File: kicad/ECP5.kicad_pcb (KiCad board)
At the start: 4 copper layers, 64.4 x 54.6 mm, 143 parts, among them J1 USB Type C, J2 USB Type C, J3 FTS-126-02-L-DV, Q1 MMST2222A, SW1 User, U1 LFE5U-25F-6BG381C, U2 IS25LP128F, U3 FT231XQ, U4 LP5907MFX-3.3, U5 FT2232HQ, U6 93LCxxBxxOT, U7 TLV62569DBVT, U8 TLV62569DBVT, U9 TLV62569DBVT, Y1 50MHz, Y2 12.000 MHz

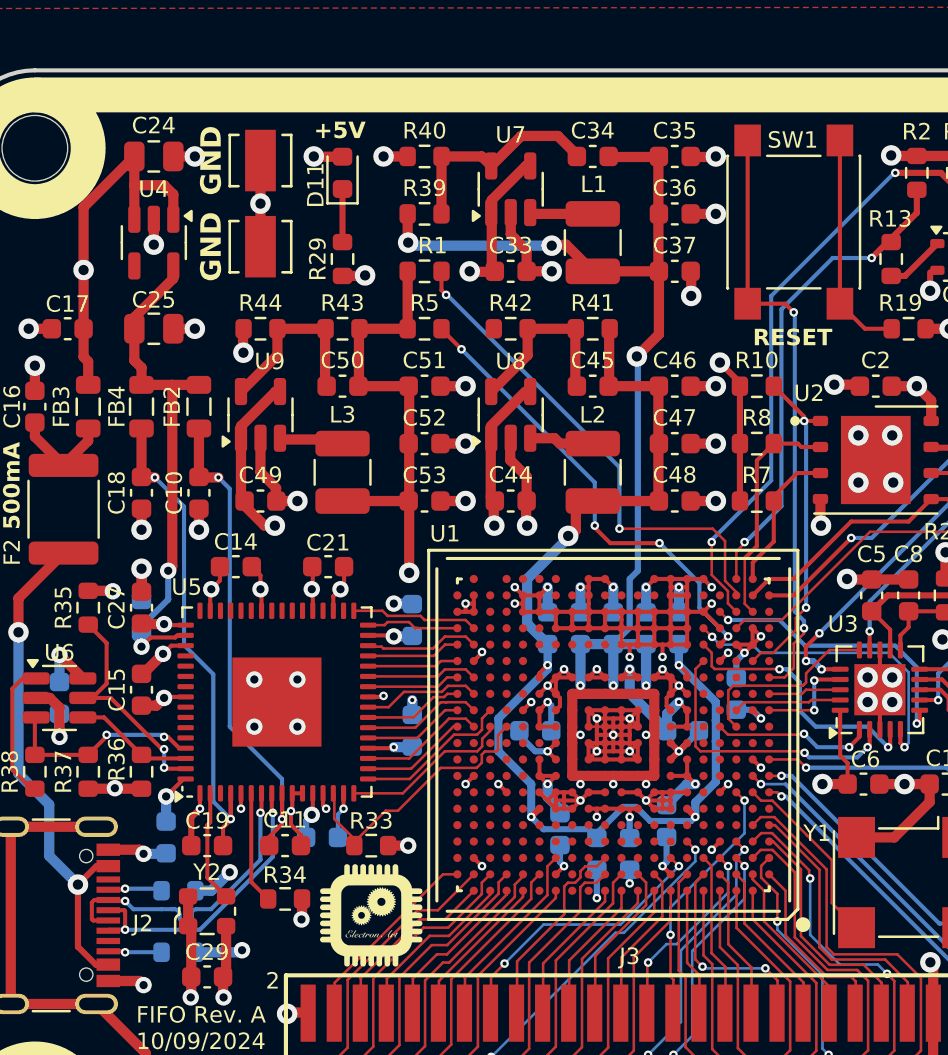
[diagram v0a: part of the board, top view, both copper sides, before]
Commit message: Updated USB D+/- routing
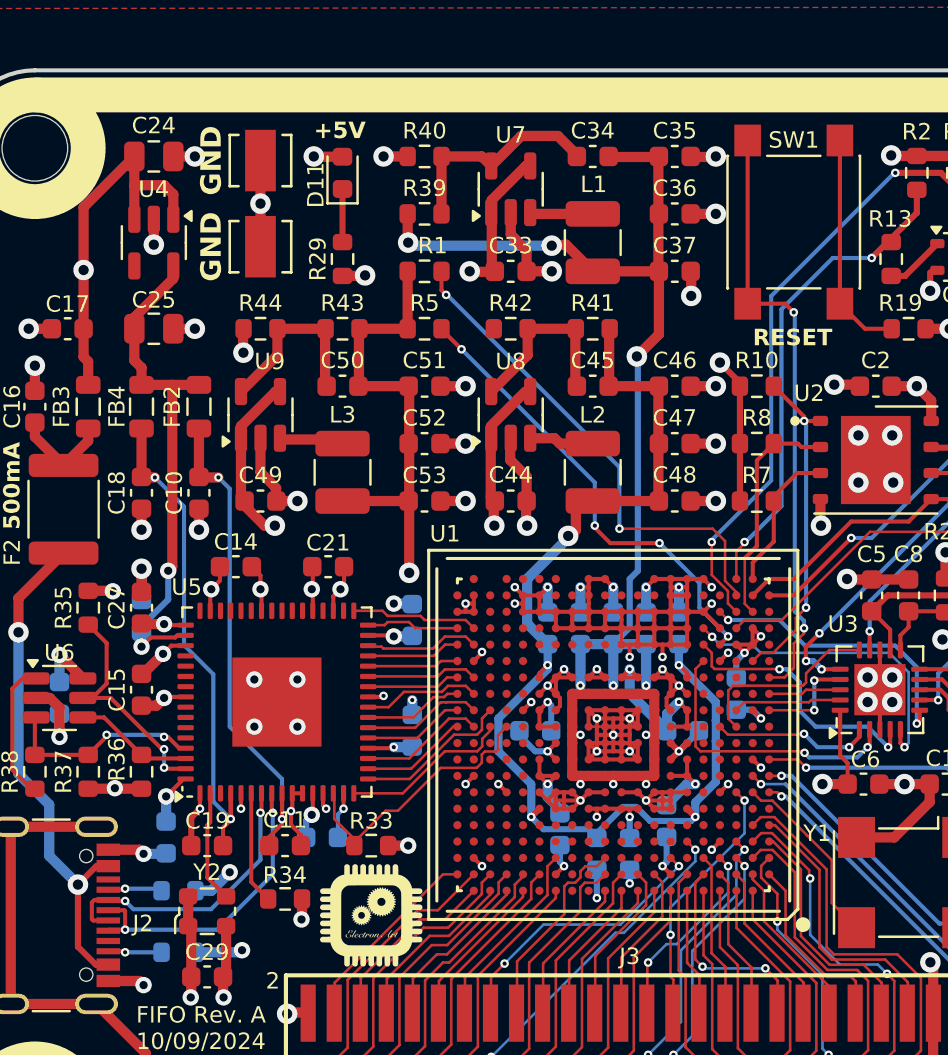
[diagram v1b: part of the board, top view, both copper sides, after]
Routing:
- net FTDI_D-: track 15.1 -> 14.4 mm
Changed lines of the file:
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@@
 		(tags "SPST Button Switch")
 		(property "Reference" "SW1"
-			(at -4 0.05 0)
+			(at -4 0 0)
 			(unlocked yes)
 			(layer "F.SilkS")
@@
 		)
 		(property "Value" "0.1µF"
-			(at 0 1.43 360)
+			(at 0 1.43 0)
 			(layer "F.Fab")
 			(effects
@@
 		)
 		(fp_text user "${REFERENCE}"
-			(at 0 0 360)
+			(at 0 0 0)
 			(layer "F.Fab")
 			(effects
@@
 		)
 		(property "Value" "2.2K"
-			(at 0 1.43 360)
+			(at 0 1.43 0)
 			(layer "F.Fab")
 			(effects
@@
 		)
 		(fp_text user "${REFERENCE}"
-			(at 0 0 360)
+			(at 0 0 0)
 			(layer "F.Fab")
 			(effects
@@
 		)
 		(fp_text user "${REFERENCE}"
-			(at 0 0 360)
+			(at 0 0 0)
 			(layer "F.Fab")
 			(effects
@@
 		)
 		(property "Value" "0.1µF"
-			(at 0 1.43 360)
+			(at 0 1.43 0)
 			(layer "F.Fab")
 			(effects
@@
 		)
 		(property "Value" "0.1µF"
-			(at 0 1.43 360)
+			(at 0 1.43 0)
 			(layer "F.Fab")
 			(effects
@@
 		)
 		(fp_text user "${REFERENCE}"
-			(at 0 0 360)
+			(at 0 0 0)
 			(layer "F.Fab")
 			(effects
@@
 		)
 		(property "Value" "0.1µF"
-			(at 0 1.43 360)
+			(at 0 1.43 0)
 			(layer "F.Fab")
 			(effects
@@
 		)
 		(fp_text user "${REFERENCE}"
-			(at 0 0 360)
+			(at 0 0 0)
 			(layer "F.Fab")
 			(effects
@@
 		)
 		(property "Value" "93LCxxBxxOT"
-			(at 0 2.4 360)
+			(at 0 2.4 0)
 			(layer "F.Fab")
 			(effects
@@
 		)
 		(fp_text user "${REFERENCE}"
-			(at 0 0 360)
+			(at 0 0 0)
 			(layer "F.Fab")
 			(effects
@@
 		)
 		(property "Value" "5.1K"
-			(at 0 -1.43 360)
+			(at 0 -1.43 0)
 			(layer "B.Fab")
 			(effects
@@
 		)
 		(property "Value" "0.1µF"
-			(at 0 -1.43 360)
+			(at 0 -1.43 0)
 			(layer "B.Fab")
 			(effects
@@
 		)
 		(fp_text user "${REFERENCE}"
-			(at 0 0 360)
+			(at 0 0 0)
 			(layer "B.Fab")
 			(effects
@@
 		)
 		(property "Value" "5.1K"
-			(at 0 -1.43 360)
+			(at 0 -1.43 0)
 			(layer "B.Fab")
 			(effects
@@
 	)
 	(segment
-		(start 122.606552 110.3)
-		(end 122.486552 110.3)
-		(width 0.2)
-		(layer "B.Cu")
-		(net 232)
-	)
-	(segment
-		(start 122.846552 110.66)
-		(end 122.846552 110.54)
-		(width 0.2)
-		(layer "B.Cu")
-		(net 232)
-	)
-	(segment
-		(start 122.486552 110.3)
-		(end 121.992515 110.3)
-		(width 0.2)
-		(layer "B.Cu")
-		(net 232)
-	)
-	(segment
-		(start 126.8 107.886712)
-		(end 124.386712 110.3)
-		(width 0.2)
-		(layer "B.Cu")
-		(net 232)
-	)
-	(segment
 		(start 120.6 110.3)
 		(end 120.2 109.9)
@@
 	)
 	(segment
-		(start 121.992515 110.3)
-		(end 120.6 110.3)
-		(width 0.2)
-		(layer "B.Cu")
-		(net 232)
-	)
-	(segment
-		(start 123.446552 110.54)
-		(end 123.446552 110.66)
-		(width 0.2)
-		(layer "B.Cu")
-		(net 232)
-	)
-	(segment
-		(start 123.206552 110.9)
-		(end 123.086552 110.9)
-		(width 0.2)
-		(layer "B.Cu")
-		(net 232)
-	)
-	(segment
-		(start 124.386712 110.3)
-		(end 123.686552 110.3)
+		(start 126.8 107.886712)
+		(end 124.386712 110.3)
 		(width 0.2)
 		(layer "B.Cu")
@@
 		(net 232)
 	)
-	(arc
-		(start 122.846552 110.54)
-		(mid 122.776258 110.370294)
-		(end 122.606552 110.3)
-		(width 0.2)
-		(layer "B.Cu")
-		(net 232)
-	)
-	(arc
-		(start 123.446552 110.66)
-		(mid 123.376258 110.829706)
-		(end 123.206552 110.9)
-		(width 0.2)
-		(layer "B.Cu")
-		(net 232)
-	)
-	(arc
-		(start 123.686552 110.3)
-		(mid 123.516846 110.370294)
-		(end 123.446552 110.54)
-		(width 0.2)
-		(layer "B.Cu")
-		(net 232)
-	)
-	(arc
-		(start 123.086552 110.9)
-		(mid 122.916846 110.829706)
-		(end 122.846552 110.66)
+	(segment
+		(start 124.386712 110.3)
+		(end 120.6 110.3)
 		(width 0.2)
 		(layer "B.Cu")
@@
 	)
 	(segment
-		(start 127.4 107.74916)
-		(end 123.84916 111.3)
-		(width 0.2)
-		(layer "B.Cu")
-		(net 233)
-	)
-	(segment
-		(start 123.84916 111.3)
+		(start 124.7 111.3)
 		(end 120.2 111.3)
 		(width 0.2)
@@
 	)
 	(segment
-		(start 127.4 105.582695)
-		(end 127.4 107.74916)
+		(start 127.4 108.6)
+		(end 124.7 111.3)
 		(width 0.2)
 		(layer "B.Cu")
@@
 	(segment
 		(start 127.4 105.6)
-		(end 127.4 105.582695)
+		(end 127.4 108.6)
 		(width 0.2)
 		(layer "B.Cu")
@@
 		)
 	)
-	(generated
-		(type tuning_pattern)
-		(name "Tuning Pattern")
-		(layer "B.Cu")
-		(base_line
-			(pts
-				(xy 123.686552 110.3) (xy 121.992515 110.3)
-			)
-		)
-		(corner_radius_percent 80)
-		(end
-			(xy 121.992515 110.3)
-		)
-		(initial_side "left")
-		(last_diff_pair_gap 0.18)
-		(last_netname "FTDI_D-")
-		(last_status "too_short")
-		(last_track_width 0.2)
-		(last_tuning "15.6827 mm (too short)")
-		(max_amplitude 0.6)
-		(min_amplitude 0)
-		(min_spacing 0.6)
-		(origin
-			(xy 123.686552 110.3)
-		)
-		(override_custom_rules no)
-		(rounded yes)
-		(single_sided no)
-		(target_length 1000000)
-		(target_length_max 1000000.1)
-		(target_length_min 999999.9)
-		(target_skew 0)
-		(target_skew_max 0.1)
-		(target_skew_min -0.1)
-		(tuning_mode "single")
-		(members 2487f087-3aac-4a66-bda5-6327e1fa3f22 2b26a126-b3eb-435b-8f4a-f1089f99072d
-			36cd9a7a-7935-4e43-ac3e-73e7b1a5498a 40a33053-0dbd-45e0-8974-fa353c070704
-			84474866-c306-4e32-822d-058b60b3c7e6 8e153df2-7bb3-4bf4-a8ca-de7ae37abfcd
-			aaa3d956-0208-4fe1-a436-eeab9a2938b5 cbec4b23-d0f2-4299-8d58-a59de2e950d6
-			ec4c1b6e-fc9b-46a4-91a6-a9cc44f7a438
-		)
-	)

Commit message: Routing complete
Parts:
- added C2: 0.1µF, Capacitor_SMD:C_0603_1608Metric, F.Cu at (166.8, 107.2)
- added Y2: 22.5792 MHz, Oscillator:Oscillator_SMD_Abracon_ASE-4Pin_3.2x2.5mm, F.Cu at (163.2, 107.2)
- F1: value Hold 750mA -> Hold 140mA
- Y1: value 50MHz -> 24.576 MHz; footprint ECP5_TX_AUDIO:Oscillator_SMD_Diodes_FN-4Pin_7.0x5.0mm -> Oscillator:Oscillator_SMD_Abracon_ASE-4Pin_3.2x2.5mm
- moved C10 4.62 mm to (164.6, 111.2)
- moved R25 3.25 mm to (167.4, 111.2)
- moved C1 3.06 mm to (159.6, 107.2), turned to 90 degrees
- moved Y1 2.84 mm to (156.2, 107.2), turned to 90 degrees
- renumbered C9 to C10, C10 to C11, C11 to C12, C12 to C13, C13 to C14, C14 to C15, C15 to C16, C16 to C17, C17 to C18, C18 to C19, C19 to C20, C20 to C21, C21 to C22, C22 to C23, C23 to C24, C24 to C25, C25 to C26, C26 to C27, C27 to C28, C28 to C29, C2 to C3, C29 to C30, C30 to C31, C31 to C32, C32 to C33, C33 to C34, C34 to C35, C35 to C36, C36 to C37, C37 to C38, C38 to C39, C3 to C4, C39 to C40, C40 to C41, C41 to C42, C42 to C43, C43 to C44, C44 to C45, C45 to C46, C46 to C47, C47 to C48, C48 to C49, C4 to C5, C49 to C50, C50 to C51, C51 to C52, C52 to C53, C53 to C54, C54 to C55, C55 to C56, C56 to C57, C5 to C6, C6 to C7, C7 to C8, C8 to C9, D7 to D5, D5 to D6, D6 to D7, R20 to R19, R21 to R20, R19 to R21, Y2 to Y3
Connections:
- net CLK_50MHz renamed CLK_24.576MHz
- U1 pad F1: unconnected-(U1F-PL26B-PadF1) -> LED_2
- U1 pad H2: LED_2 -> CLK_22.5792MHz
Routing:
- net CLK_22.5792MHz: track 0.00 -> 12.8 mm
- net CLK_24.576MHz: track 9.02 -> 5.22 mm
- net +3V3: track 116.1 -> 118.9 mm, vias 27 -> 28
- net EXT_1: track 19.8 -> 18.2 mm
- net EXT_0: track 13.6 -> 12.1 mm
- net LED_2: track 18.8 -> 17.6 mm, vias 2 -> 0
- net Net-(J1-SHIELD): track 27.4 -> 26.2 mm
- net EXT_3: track 17.7 -> 16.7 mm, vias 2 -> 0
- net EXT_2: track 11.7 -> 10.7 mm
- net EXT_5: track 16.1 -> 15.3 mm
- net GND: track 267.1 -> 267.9 mm
- net EXT_4: track 9.17 -> 8.48 mm
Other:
- board text added: "USB Audio Rev. A 10/09/2024"
- board text removed: "FIFO Rev. A 10/09/2024"

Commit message: PCB changes
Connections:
- net FT2232_RESET renamed ~{FT2232_RESET}
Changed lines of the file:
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@@
 	(net 306 "unconnected-(U5-~{PWREN}-Pad60)")
 	(net 307 "Net-(U5-OSCI)")
-	(net 308 "FT2232_RESET")
+	(net 308 "~{FT2232_RESET}")
 	(net 309 "Net-(D3-A)")
 	(net 310 "Net-(D4-A)")
@@
 		(tags "SOT TO_SOT_SMD")
 		(property "Reference" "U9"
-			(at 2.6 0.45 0)
+			(at 2.6 0.4 0)
 			(unlocked yes)
 			(layer "F.SilkS")
@@
 			(layers "F.Cu" "F.Paste" "F.Mask")
 			(roundrect_rratio 0.25)
-			(net 308 "FT2232_RESET")
+			(net 308 "~{FT2232_RESET}")
 			(pintype "passive")
 		)
@@
 		(tags "capacitor")
 		(property "Reference" "C10"
-			(at 0.6 1.3 90)
+			(at 0 1.3 90)
 			(unlocked yes)
 			(layer "F.SilkS")
@@
 			(size 0.4 0.4)
 			(layers "F.Cu" "F.Paste" "F.Mask")
-			(net 308 "FT2232_RESET")
+			(net 308 "~{FT2232_RESET}")
 			(pinfunction "PR29B")
 			(pintype "bidirectional")
@@
 			(layers "F.Cu" "F.Paste" "F.Mask")
 			(roundrect_rratio 0.25)
-			(net 308 "FT2232_RESET")
+			(net 308 "~{FT2232_RESET}")
 			(pinfunction "~{RESET}")
 			(pintype "input")
@@
 		(tags "SOT TO_SOT_SMD")
 		(property "Reference" "U6"
-			(at 0 -2.2 0)
+			(at 1.1 -2.2 0)
 			(unlocked yes)
 			(layer "F.SilkS")
@@
 		(tags "resistor")
 		(property "Reference" "R31"
-			(at 0 1.4 180)
+			(at 0 1.3 180)
 			(unlocked yes)
 			(layer "B.SilkS")
@@
 		(tags "resistor")
 		(property "Reference" "R32"
-			(at 0 1.43 180)
+			(at 0 1.3 180)
 			(unlocked yes)
 			(layer "B.SilkS")

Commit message: Changed the name of the project path
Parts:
- F1, F2: footprint ECP5_TX_AUDIO:Fuse_1812_4532Metric -> ECP5_BGA381_FT2232HQ_FIFO:Fuse_1812_4532Metric
- J1, J2: footprint ECP5_TX_AUDIO:USB_C_Receptacle_GCT_USB4105-xx-A_16P_TopMnt_Horizontal -> ECP5_BGA381_FT2232HQ_FIFO:USB_C_Receptacle_GCT_USB4105-xx-A_16P_TopMnt_Horizontal
- J3: footprint ECP5_TX_AUDIO:SAMTEC-FTS-126-02-X-DV -> ECP5_BGA381_FT2232HQ_FIFO:SAMTEC-FTS-126-02-X-DV
- TP1, TP2: footprint ECP5_TX_AUDIO:KEYSTONE_5197TR -> ECP5_BGA381_FT2232HQ_FIFO:KEYSTONE_5197TR
- U1: footprint ECP5_TX_AUDIO:BGA-381_pitch0.8mm_dia0.4mm -> ECP5_BGA381_FT2232HQ_FIFO:BGA-381_pitch0.8mm_dia0.4mm
- U2: footprint ECP5_TX_AUDIO:WSON-8-1EP_6x5mm_P1.27mm_EP3.4x4.3mm -> ECP5_BGA381_FT2232HQ_FIFO:WSON-8-1EP_6x5mm_P1.27mm_EP3.4x4.3mm
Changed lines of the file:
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@@
 		)
 	)
-	(footprint "ECP5_TX_AUDIO:WSON-8-1EP_6x5mm_P1.27mm_EP3.4x4.3mm"
+	(footprint "ECP5_BGA381_FT2232HQ_FIFO:WSON-8-1EP_6x5mm_P1.27mm_EP3.4x4.3mm"
 		(layer "F.Cu")
 		(at 156.8 88.4)
@@
 			)
 		)
-		(property "Footprint" "ECP5_TX_AUDIO:WSON-8-1EP_6x5mm_P1.27mm_EP3.4x4.3mm"
+		(property "Footprint" "ECP5_BGA381_FT2232HQ_FIFO:WSON-8-1EP_6x5mm_P1.27mm_EP3.4x4.3mm"
 			(at 0 0 0)
 			(layer "F.Fab")
@@
 			(pintype "power_in")
 		)
-		(model "${ECP5_TX_AUDIO}/3dmodels/WSON8-6x5.STEP"
+		(model "${ECP5_BGA381_FT2232HQ_FIFO}/3dmodels/WSON8-6x5.STEP"
 			(offset
 				(xyz 0 0 0)
@@
 		)
 	)
-	(footprint "ECP5_TX_AUDIO:SAMTEC-FTS-126-02-X-DV"
+	(footprint "ECP5_BGA381_FT2232HQ_FIFO:SAMTEC-FTS-126-02-X-DV"
 		(layer "F.Cu")
 		(at 145 117.4)
 		(descr "translated Allegro footprint")
 		(property "Reference" "J3"
-			(at -0.2 -4.8 0)
+			(at 0 -4.8 0)
 			(unlocked yes)
 			(layer "F.SilkS")
@@
 			)
 		)
-		(property "Footprint" "ECP5_TX_AUDIO:SAMTEC-FTS-126-02-X-DV"
+		(property "Footprint" "ECP5_BGA381_FT2232HQ_FIFO:SAMTEC-FTS-126-02-X-DV"
 			(at 0 0 0)
 			(layer "F.Fab")
@@
 		)
 		(fp_text user "1"
-			(at -17.7 2.8 0)
+			(at -17.9 2.667 0)
 			(layer "F.SilkS")
 			(effects
@@
 			)
 		)
-		(fp_text user "51"
-			(at 18 2.7 0)
+		(fp_text user "2"
+			(at -17.8 -3.2 0)
 			(layer "F.SilkS")
 			(effects
@@
 		)
 		(fp_text user "52"
-			(at 18 -3.7 0)
+			(at 18.1 -3.9 0)
 			(layer "F.SilkS")
 			(effects
@@
 			)
 		)
-		(fp_text user "2"
-			(at -17.6 -3.6 0)
+		(fp_text user "51"
+			(at 18 2.667 0)
 			(layer "F.SilkS")
 			(effects
@@
 			)
 		)
-		(fp_text user "33.020"
-			(at -0.8 5.906 0)
+		(fp_text user "1.270"
+			(at -18.504 -4.826 0)
 			(layer "Dwgs.User")
 			(effects
@@
 			)
 		)
-		(fp_text user "31.750"
-			(at -0.8 -5.842 0)
+		(fp_text user "4.064"
+			(at -21.552 0.127 0)
 			(layer "Dwgs.User")
 			(effects
@@
 			)
 		)
-		(fp_text user "1.270"
-			(at -18.504 -4.826 0)
+		(fp_text user "3.429"
+			(at -24.981 0.127 0)
 			(layer "Dwgs.User")
 			(effects
@@
 			)
 		)
-		(fp_text user "4.064"
-			(at -21.552 0.127 0)
+		(fp_text user "33.020"
+			(at -0.8 5.906 0)
 			(layer "Dwgs.User")
 			(effects
@@
 			)
 		)
-		(fp_text user "3.429"
-			(at -24.981 0.127 0)
+		(fp_text user "31.750"
+			(at -0.8 -5.842 0)
 			(layer "Dwgs.User")
 			(effects
@@
 			)
 		)
-		(fp_text user "1"
-			(at -18.33 2.667 0)
+		(fp_text user "2"
+			(at -18.33 -1.397 0)
 			(layer "F.Fab")
 			(effects
@@
 			)
 		)
-		(fp_text user "51"
-			(at 17.301 2.667 0)
+		(fp_text user "1"
+			(at -18.33 2.667 0)
 			(layer "F.Fab")
 			(effects
@@
 			)
 		)
-		(fp_text user "2"
-			(at -18.33 -1.397 0)
+		(fp_text user "51"
+			(at 17.301 2.667 0)
 			(layer "F.Fab")
 			(effects
@@
 			(pintype "passive")
 		)
-		(model "${ECP5_TX_AUDIO}/3dmodels/SAMTEC-FTS-126-02-X-DV.step"
+		(model "${ECP5_BGA381_FT2232HQ_FIFO}/3dmodels/SAMTEC-FTS-126-02-X-DV.step"
 			(offset
 				(xyz 0 0 0.5)
@@
 		)
 	)
-	(footprint "ECP5_TX_AUDIO:Fuse_1812_4532Metric"
+	(footprint "ECP5_BGA381_FT2232HQ_FIFO:Fuse_1812_4532Metric"
 		(layer "F.Cu")
 		(at 170.6 91.8 -90)
@@
 			)
 		)
-		(property "Footprint" "ECP5_TX_AUDIO:Fuse_1812_4532Metric"
+		(property "Footprint" "ECP5_BGA381_FT2232HQ_FIFO:Fuse_1812_4532Metric"
 			(at 0 0 -90)
 			(layer "F.Fab")
@@
 			(pintype "passive")
 		)
-		(model "${ECP5_TX_AUDIO}/3dmodels/0ZCG-0_70mm.STEP"
+		(model "${ECP5_BGA381_FT2232HQ_FIFO}/3dmodels/0ZCG-0_70mm.STEP"
 			(offset
 				(xyz 0 0 0)
@@
 		)
 	)
-	(footprint "ECP5_TX_AUDIO:USB_C_Receptacle_GCT_USB4105-xx-A_16P_TopMnt_Horizontal"
+	(footprint "ECP5_BGA381_FT2232HQ_FIFO:USB_C_Receptacle_GCT_USB4105-xx-A_16P_TopMnt_Horizontal"
 		(layer "F.Cu")
 		(at 167.1725 100.9 90)
@@
 		(tags "USB C Type-C Receptacle SMD USB 2.0 16P 16C USB4105-15-A USB4105-15-A-060 USB4105-15-A-120 USB4105-GF-A USB4105-GF-A-060 USB4105-GF-A-120")
 		(property "Reference" "J1"
-			(at 0.3 -0.1725 90)
+			(at 0.3 -0.2725 90)
 			(unlocked yes)
 			(layer "F.SilkS")
@@
 			)
 		)
-		(property "Footprint" "ECP5_TX_AUDIO:USB_C_Receptacle_GCT_USB4105-xx-A_16P_TopMnt_Horizontal"
+		(property "Footprint" "ECP5_BGA381_FT2232HQ_FIFO:USB_C_Receptacle_GCT_USB4105-xx-A_16P_TopMnt_Horizontal"
 			(at 0.3 5.5 90)
 			(layer "F.Fab")
@@
 			)
 		)
-		(property "Description" "CONN RCP USB2.0 TYP C 24P SMD RA"
+		(property "Description" "USB 2.0-only Type-C Receptacle connector"
 			(at 0.3 -2.4 90)
 			(layer "F.Fab")
@@
 		)
 	)
-	(footprint "ECP5_TX_AUDIO:KEYSTONE_5197TR"
+	(footprint "ECP5_BGA381_FT2232HQ_FIFO:KEYSTONE_5197TR"
 		(layer "F.Cu")
 		(at 126.8 73.8 90)
 		(property "Reference" "TP2"
-			(at -0.2 -2.4 90)
+			(at 1.425 -3.385 90)
 			(unlocked yes)
 			(layer "F.SilkS")
@@
 			)
 		)
-		(property "Footprint" "ECP5_TX_AUDIO:KEYSTONE_5197TR"
+		(property "Footprint" "ECP5_BGA381_FT2232HQ_FIFO:KEYSTONE_5197TR"
 			(at 0 0 90)
 			(layer "F.Fab")
@@
 			(solder_mask_margin 0.102)
 		)
-		(model "${ECP5_TX_AUDIO}/3dmodels/5197TR.step"
+		(model "${ECP5_BGA381_FT2232HQ_FIFO}/3dmodels/5197TR.step"
 			(offset
 				(xyz -1.45 2.3 -0.5)
@@
 		)
 	)
-	(footprint "ECP5_TX_AUDIO:BGA-381_pitch0.8mm_dia0.4mm"
+	(footprint "ECP5_BGA381_FT2232HQ_FIFO:BGA-381_pitch0.8mm_dia0.4mm"
 		(layer "F.Cu")
 		(at 144 101.8 180)
 		(property "Reference" "U1"
-			(at 8.2 9.8 0)
+			(at 7.8 9.6 0)
 			(unlocked yes)
 			(layer "F.SilkS")
@@
 			)
 		)
-		(property "Footprint" "ECP5_TX_AUDIO:BGA-381_pitch0.8mm_dia0.4mm"
+		(property "Footprint" "ECP5_BGA381_FT2232HQ_FIFO:BGA-381_pitch0.8mm_dia0.4mm"
 			(at 0 0 180)
 			(layer "F.Fab")
@@
 			(solder_paste_margin -0.025)
 		)
-		(model "${ECP5_TX_AUDIO}/3dmodels/LFE5UM-85F-8BG381C.STEP"
+		(model "${ECP5_BGA381_FT2232HQ_FIFO}/3dmodels/LFE5UM-85F-8BG381C.STEP"
 			(offset
 				(xyz 0 0 0)
@@
 		(property "Reference" "Y2"
 			(at 0 -2.2 90)
+			(unlocked yes)
 			(layer "F.SilkS")
 			(effects
@@
 		(property "Reference" "C2"
 			(at 0 -1.225 90)
+			(unlocked yes)
 			(layer "F.SilkS")
 			(effects
@@
 			)
 		)
-		(property "Description" "IC USB SERIAL FULL UART 20QFN"
+		(property "Description" "Full Speed USB to Full Handshake UART, QFN-20"
 			(at 0 0 90)
 			(unlocked yes)
@@
 		(property "Reference" "Y1"
 			(at 0 -2.2 90)
+			(unlocked yes)
 			(layer "F.SilkS")
 			(effects
@@
 		)
 	)
-	(footprint "ECP5_TX_AUDIO:USB_C_Receptacle_GCT_USB4105-xx-A_16P_TopMnt_Horizontal"
+	(footprint "ECP5_BGA381_FT2232HQ_FIFO:USB_C_Receptacle_GCT_USB4105-xx-A_16P_TopMnt_Horizontal"
 		(layer "F.Cu")
 		(at 121.2 110.3 -90)
@@
 		(tags "USB C Type-C Receptacle SMD USB 2.0 16P 16C USB4105-15-A USB4105-15-A-060 USB4105-15-A-120 USB4105-GF-A USB4105-GF-A-060 USB4105-GF-A-120")
 		(property "Reference" "J2"
-			(at 0.7 0.1275 0)
+			(at 0.3 0.1 0)
 			(unlocked yes)
 			(layer "F.SilkS")
@@
 			)
 		)
-		(property "Footprint" "ECP5_TX_AUDIO:USB_C_Receptacle_GCT_USB4105-xx-A_16P_TopMnt_Horizontal"
-			(at 0.3 5.5 90)
+		(property "Footprint" "ECP5_BGA381_FT2232HQ_FIFO:USB_C_Receptacle_GCT_USB4105-xx-A_16P_TopMnt_Horizontal"
+			(at 0.3 5.5 -90)
 			(layer "F.Fab")
 			(hide yes)
@@
 		)
 		(property "Datasheet" "https://www.usb.org/sites/default/files/documents/usb_type-c.zip"
-			(at 0.3 5.5 90)
+			(at 0.3 5.5 -90)
 			(layer "F.Fab")
 			(hide yes)
@@
 			)
 		)
-		(property "Description" "CONN RCP USB2.0 TYP C 24P SMD RA"
-			(at 0.3 -2.4 90)
+		(property "Description" "USB 2.0-only Type-C Receptacle connector"
+			(at 0.3 -2.4 -90)
 			(layer "F.Fab")
 			(hide yes)
@@
 		)
 		(property "MPN" "USB4105-GF-A-120"
-			(at 0.3 12.8 90)
+			(at 0.3 12.8 -90)
 			(layer "F.Fab")
 			(hide yes)
@@
 		)
 		(property "Manufacturer" "GCT"
-			(at 0.2 14.9 90)
+			(at 0.2 14.9 -90)
 			(layer "F.Fab")
 			(hide yes)
@@
 		)
 	)
-	(footprint "ECP5_TX_AUDIO:Fuse_1812_4532Metric"
+	(footprint "ECP5_BGA381_FT2232HQ_FIFO:Fuse_1812_4532Metric"
 		(layer "F.Cu")
 		(at 117.2 90.8 -90)
@@
 		(tags "fuse")
 		(property "Reference" "F2"
-			(at 2.1 2.5 90)
+			(at 1.9 2.5 90)
 			(unlocked yes)
 			(layer "F.SilkS")
@@
 			)
 		)
-		(property "Footprint" "ECP5_TX_AUDIO:Fuse_1812_4532Metric"
-			(at 0 0 90)
+		(property "Footprint" "ECP5_BGA381_FT2232HQ_FIFO:Fuse_1812_4532Metric"
+			(at 0 0 -90)
 			(layer "F.Fab")
 			(hide yes)
@@
 		)
 		(property "Datasheet" ""
-			(at 0 0 90)
+			(at 0 0 -90)
 			(layer "F.Fab")
 			(hide yes)
@@
 		)
 		(property "Description" "PTC RESET FUSE 30V 500MA 1812"
-			(at 0 0 90)
+			(at 0 0 -90)
 			(layer "F.Fab")
 			(hide yes)
@@
 		)
 		(property "MPN" "0ZCG0050AF2C"
-			(at 0 0 90)
+			(at 0 0 -90)
 			(layer "F.Fab")
 			(hide yes)
@@
 		)
 		(property "Manufacturer" "Bel Fuse Inc."
-			(at 0 0 90)
+			(at 0 0 -90)
 			(layer "F.Fab")
 			(hide yes)
@@
 			(pintype "passive")
 		)
-		(model "${ECP5_TX_AUDIO}/3dmodels/0ZCG-0_70mm.STEP"
+		(model "${ECP5_BGA381_FT2232HQ_FIFO}/3dmodels/0ZCG-0_70mm.STEP"
 			(offset
 				(xyz 0 0 0)
@@
 		)
 	)
-	(footprint "ECP5_TX_AUDIO:KEYSTONE_5197TR"
+	(footprint "ECP5_BGA381_FT2232HQ_FIFO:KEYSTONE_5197TR"
 		(layer "F.Cu")
 		(at 126.8 78 90)
 		(property "Reference" "TP1"
-			(at 0 -2.2 90)
+			(at 1.425 -3.385 90)
 			(unlocked yes)
 			(layer "F.SilkS")
@@
 			)
 		)
-		(property "Footprint" "ECP5_TX_AUDIO:KEYSTONE_5197TR"
+		(property "Footprint" "ECP5_BGA381_FT2232HQ_FIFO:KEYSTONE_5197TR"
 			(at 0 0 90)
 			(layer "F.Fab")
@@
 			(solder_mask_margin 0.102)
 		)
-		(model "${ECP5_TX_AUDIO}/3dmodels/5197TR.step"
+		(model "${ECP5_BGA381_FT2232HQ_FIFO}/3dmodels/5197TR.step"
 			(offset
 				(xyz -1.45 2.3 -0.5)
